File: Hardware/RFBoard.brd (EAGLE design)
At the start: 100 x 100 mm, 327 parts, among them IC1 HMC1097, IC10 NCP702-1.8, IC11 QPC6082, IC12 MCP4812, IC13 QPC6082, IC14 LT5560, IC15 ADF4360, IC16 HMC284, IC17 HMC284, IC18 NCP702-3.3, IC19 NCP702-3.3, IC2 MAX2871, IC20 LT1395, IC21 MAADSS0008, IC22 MAADSS0008, IC23 MAADSS0008, IC24 RFSA2033, IC25 MMG3H21NT1, IC26 MMG3H21NT1, IC27 HMC1021, IC28 MCP4812, IC29 NCP702-3.3, IC3 AP2114HA-3.3, IC30 NCP702-3.3, IC4 NCP702-3.3, IC5 NCP702-3.3, IC6 MAX5873, IC7 NCP702-1.8, IC8 NCP702-3.3, IC9 NCP702-3.3, Q1 BSS123, Q2 BSS123, Q3 BSS123, Q4 BSS123, Q5 BSS123, X1 out

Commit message: Almost all RF routing
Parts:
- removed C157, C158: 1u, rcl:C0603
- removed C22, C23, C24: 33p, rcl:C0603
- removed IC11, IC13: QPC6082, rf:QFN40P200X200X60-15T98
- removed IC30: NCP702-3.3, rf:SOT95P240X110-5
- removed R15, R5, R6: 33, resistor:R0603
- added IC31, IC32: QPC6064, rf:QFN50P400X400X75-25T270
- added L68, L69: (no value), rcl:L2012C
- moved R58 36.4 mm to (15.4, 52.1), flipped to the bottom
- moved R57 29.4 mm to (14.2, 49.0), flipped to the bottom
- moved R56 26.3 mm to (12.0, 49.0), flipped to the bottom, turned to 270 degrees
- moved R55 23.8 mm to (12.8, 51.5), flipped to the bottom, turned to 180 degrees
- moved C60 15.0 mm to (41.0, 86.0), turned to 180 degrees
- moved R16 14.4 mm to (51.8, 50.2)
- moved C29 14.0 mm to (94.0, 51.0), turned to 180 degrees
- moved C59 10.8 mm to (91.5, 69.5), turned to 0 degrees
- moved R54 10.1 mm to (18.0, 40.0), flipped to the bottom
- moved R3 9.63 mm to (51.8, 48.5)
- moved C10 9.51 mm to (65.0, 49.5)
- moved Q1 8.80 mm to (5.50, 73.7)
- moved Q2 6.70 mm to (5.50, 80.0)
- moved C19 6.20 mm to (49.0, 55.0)
- moved R31 5.90 mm to (5.00, 83.6)
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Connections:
- removed net N$19: C22.2, IC2.1, R5.2
- removed net N$21: C24.2, IC2.3, R15.2
- removed net N$24: C23.2, IC2.2, R6.2
- removed net N$89: IC11.8, IC13.10
- removed net STEPPED37: IC11.11, IC13.7
- new net ETOUT: IC27.6
- new net VDD2: C59.1, IC31.16, L68.2
- net +5V: now also L68.1, L69.1; no longer C158.1, IC30.1, IC30.3
- net FILTERED: now also IC32.22; no longer IC13.9
- net GND: now also IC16.9, IC17.9, IC31.1, IC31.10, IC31.12, IC31.13, IC31.15, IC31.20, IC31.21, IC31.23, IC31.25, IC31.3, IC31.4, IC31.6, IC31.7, IC31.9, IC32.1, IC32.10, IC32.12, IC32.13, IC32.15, IC32.20, IC32.21, IC32.23, IC32.25, IC32.3, IC32.4, IC32.6, IC32.7, IC32.9; no longer C157.2, C158.2, C22.1, C23.1, C24.1, IC11.14, IC11.15, IC13.14, IC13.15, IC30.2
- net MOD_OUT: now also IC31.22; no longer IC11.9
- net N$52: now also IC31.2; no longer IC11.12
- net N$53: now also IC32.11; no longer IC13.6
- net N$60: now also IC31.5; no longer IC11.13
- net N$69: now also IC32.5; no longer IC13.13
- net N$76: now also IC31.11; no longer IC11.6
- net N$77: now also IC32.2; no longer IC13.12
- net N$84: now also IC31.14; no longer IC11.7
- net N$85: now also IC32.24; no longer IC13.11
- net N$90: now also IC31.8; no longer IC11.5
- net N$91: now also IC32.8; no longer IC13.5
- net SPI_CLK: now also IC2.1; no longer R5.1
- net SPI_MOSI: now also IC2.2; no longer R6.1
- net STEPPED25: now also IC31.24, IC32.14; no longer IC11.10, IC13.8
- net SW1_CTL1: now also IC31.17; no longer IC11.3
- net SW1_CTL2: now also IC31.18; no longer IC11.2
- net SW1_CTL3: now also IC31.19; no longer IC11.1
- net SW2_CTL1: now also IC32.17; no longer IC13.3
- net SW2_CTL2: now also IC32.18; no longer IC13.2
- net SW2_CTL3: now also IC32.19; no longer IC13.1
- net SWITCHES_VCC: now also IC32.16, L69.2; no longer C157.1, C59.1, IC11.4, IC13.4, IC30.5
- net SYNTH_LE: now also IC2.3; no longer R15.1
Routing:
- net GND: track 0.00 -> 1922.2 mm, vias 0 -> 102
- net +5V: track 0.00 -> 70.8 mm, vias 0 -> 21
- net EN_DIREKT: track 0.00 -> 60.9 mm, vias 0 -> 2
- net SPI_MOSI: track 0.00 -> 51.4 mm, vias 0 -> 7
- net 15DB1: track 0.00 -> 49.6 mm, vias 0 -> 2
- net SPI_CLK: track 0.00 -> 47.4 mm, vias 0 -> 7
- net GAIN_CTRL: track 0.00 -> 45.9 mm, vias 0 -> 2
- net 15DB2: track 0.00 -> 41.3 mm, vias 0 -> 2
- net N$154: track 0.00 -> 39.1 mm, vias 0 -> 4
- net STEPPED37: track 34.1 -> 0.00 mm
- net 15DB3: track 0.00 -> 32.8 mm, vias 0 -> 2
- net N$152: track 0.00 -> 31.9 mm
- net SW_HET: track 0.00 -> 29.1 mm, vias 0 -> 2
- net SW_DIRECT: track 0.00 -> 28.9 mm, vias 0 -> 2
- net PLL_DIG3: track 0.00 -> 27.2 mm, vias 0 -> 4
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- added copper zone on layer 15, net +5V
- added copper zone on layer 1, net GND
- added copper zone on layer 16, net GND
- added copper zone on layer 2, net GND

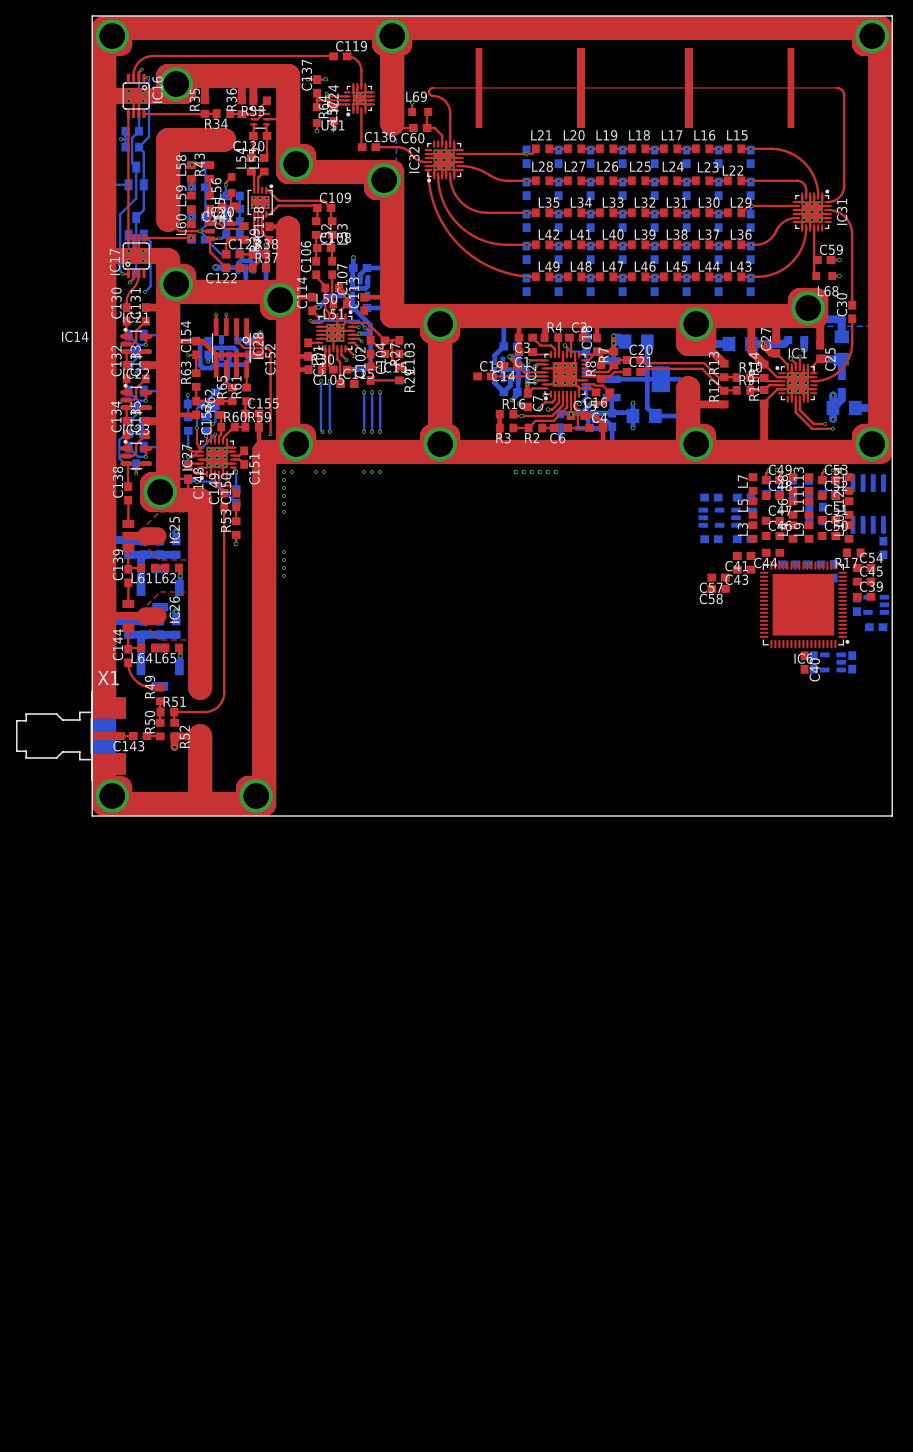
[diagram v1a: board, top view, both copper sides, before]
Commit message: FPGA + power supply added
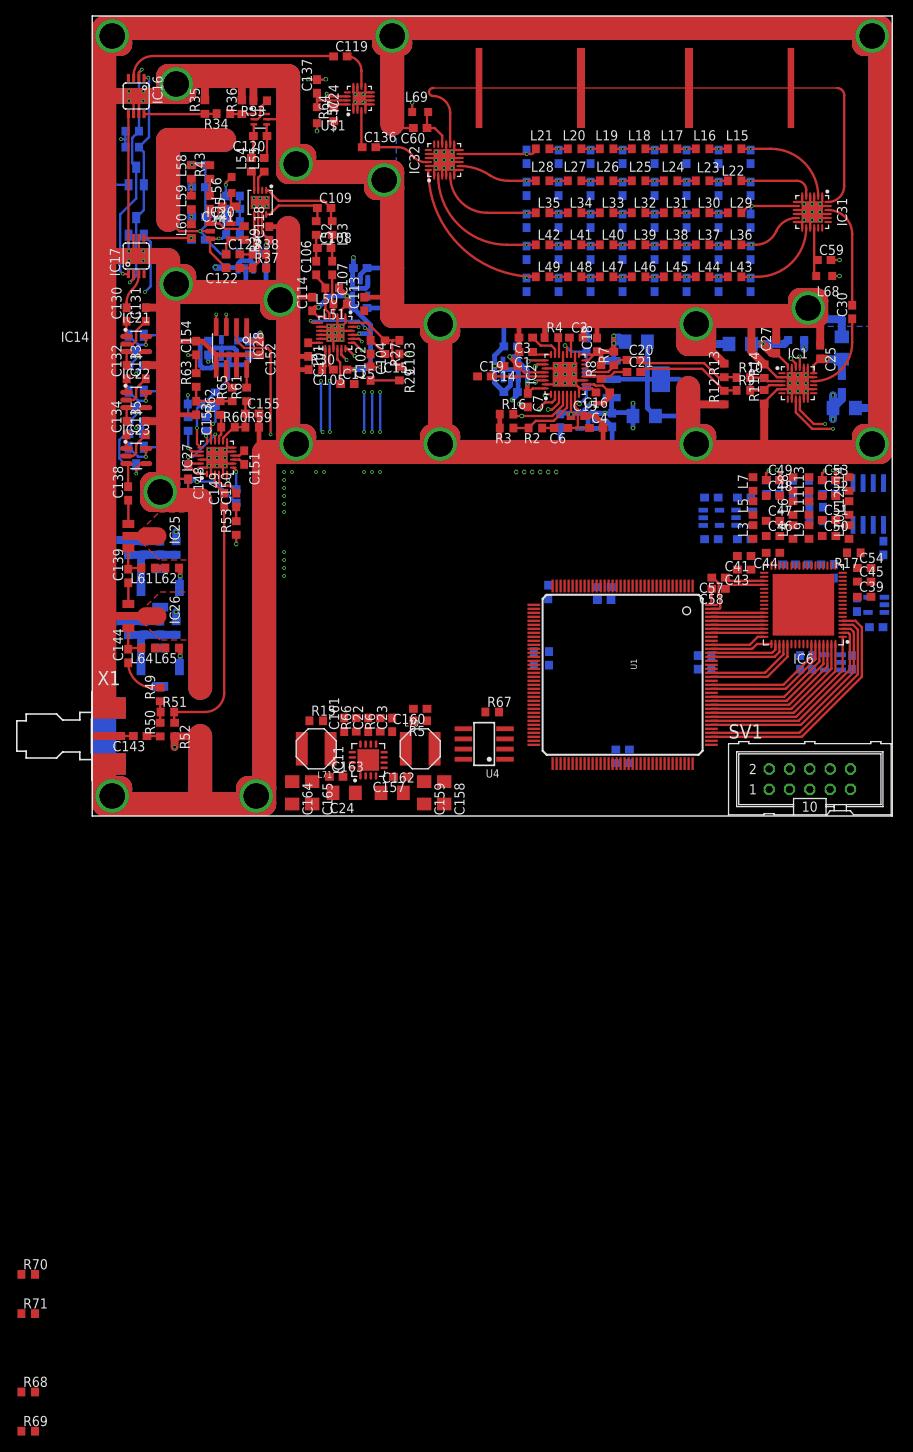
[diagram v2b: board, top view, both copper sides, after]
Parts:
- added C157, C163, C166, C167, C168, C169, C170, C171, C172, C173, C174: 100n, rcl:C0603
- added C158, C159, C164, C165: 22u, rcl:C1206
- added C160: 22p, rcl:C0603
- added C161, C23: 10n, rcl:C0603
- added C162, C24: 10u, rcl:C1206
- added C22: 1u, rcl:C0603
- added IC11: TPS42951, custom-ic:QFN65P400X400X100-17T270
- added L70, L71: 2u2, custom-ic:SRN5040
- added R15, R5: 73k2, resistor:R0603
- added R6, R66: 22k1, resistor:R0603
- added R67: 22, resistor:R0603
- added R68, R69, R70, R71: 10k, resistor:R0603
- added SV1: (no value), con-ml:ML10
- added U1: 6SLX9TQG144, xilinx_devices_V6:TQ144
- added U4: W25Q16BVSN, memory-winbond:SO08
- moved C40 0.55 mm to (88.5, 19.2), flipped to the bottom
- moved C31 0.20 mm to (90.0, 19.2)
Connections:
- new net +3V3: C158.1, C159.1, C160.1, C166.1, C167.1, C168.1, C169.1, C170.1, L70.P$2, R5.1, R68.2, R70.2, R71.2, SV1.4, U1.P122, U1.P125, U1.P129, U1.P135, U1.P20, U1.P36, U1.P42, U1.P53, U1.P63, U1.P69, U1.P90, U4.3, U4.7, U4.8
- new net FLACH_MOSI: U1.P64, U4.5
- new net FLASH_CLK: U1.P70, U4.6
- new net FLASH_CS: U1.P38, U4.1
- new net FLASH_MISO: R67.1, U4.2
- new net N$165: C22.1, IC11.11
- new net N$166: C23.1, IC11.8
- new net N$167: C160.2, IC11.9, R5.2, R6.1
- new net N$168: C161.1, IC11.13
- new net N$169: C157.1, IC11.5, L70.P$1
- new net N$170: C157.2, IC11.4
- new net N$171: IC11.12, R15.2, R66.1
- new net N$172: C163.1, IC11.16, L71.P$1
- new net N$173: C163.2, IC11.1
- new net N$174: R67.2, U1.P65
- new net N$175: R70.1, U1.P71
- new net N$176: R68.1, U1.P37
- new net N$177: R71.1, U1.P39
- new net N$19: SV1.3, U1.P106
- new net N$21: SV1.5, U1.P107
- new net N$24: SV1.9, U1.P110
- new net N$89: SV1.1, U1.P109
- new net VCCINT: C164.1, C165.1, C171.1, C172.1, C173.1, C174.1, L71.P$2, R15.1, U1.P128, U1.P19, U1.P28, U1.P52, U1.P89
- net +5V: now also C162.1, C24.1, IC11.14, IC11.2, IC11.3, IC11.7
- net CLKN: now also U1.P143
- net CLKP: now also R69.2, U1.P144
- net GND: now also C158.2, C159.2, C161.2, C162.2, C164.2, C165.2, C166.2, C167.2, C168.2, C169.2, C170.2, C171.2, C172.2, C173.2, C174.2, C22.2, C23.2, C24.2, IC11.10, IC11.15, IC11.17, IC11.6, R6.2, R66.2, R69.1, SV1.10, SV1.2, U1.P108, U1.P113, U1.P13, U1.P130, U1.P136, U1.P25, U1.P3, U1.P49, U1.P54, U1.P60, U1.P68, U1.P73, U1.P77, U1.P91, U1.P96, U4.4
- net I0: now also U1.P126
- net I1: now also U1.P127
- net I10: now also U1.P141
- net I11: now also U1.P142
- net I2: now also U1.P131
- net I3: now also U1.P132
- net I4: now also U1.P133
- net I5: now also U1.P134
- net I6: now also U1.P137
- net I7: now also U1.P138
- net I8: now also U1.P139
- net I9: now also U1.P140
- net Q0: now also U1.P111
- net Q1: now also U1.P112
- net Q10: now also U1.P123
- net Q11: now also U1.P124
- net Q2: now also U1.P114
- net Q3: now also U1.P115
- net Q4: now also U1.P116
- net Q5: now also U1.P117
- net Q6: now also U1.P118
- net Q7: now also U1.P119
- net Q8: now also U1.P120
- net Q9: now also U1.P121
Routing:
- net Q0: track 0.00 -> 30.8 mm
- net Q1: track 0.00 -> 29.1 mm
- net Q2: track 0.00 -> 27.1 mm
- net Q3: track 0.00 -> 25.3 mm
- net Q4: track 0.00 -> 23.0 mm
- net Q5: track 0.00 -> 21.0 mm
- net Q6: track 0.00 -> 20.2 mm
- net Q7: track 0.00 -> 19.3 mm
- net Q8: track 0.00 -> 18.4 mm
- net Q9: track 0.00 -> 17.5 mm
- net Q10: track 0.00 -> 16.4 mm
- net Q11: track 0.00 -> 15.5 mm
- net I0: track 0.00 -> 12.1 mm
- net I1: track 0.00 -> 11.2 mm
- net I2: track 0.00 -> 9.74 mm
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
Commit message: MCU added
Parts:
- added C175, C176, C177, C178, C179, C180: 100n, rcl:C0603
- added IC13: STM32F030C8T, micro-stm_v3:LQFP48
- added JP1: (no value), pinhead:1X05
- added JP2: (no value), pinhead:1X03
- added Q6: BSS84, transistor-small-signal:SOT23
- added R72, R73: 10k, resistor:R0603
- added SV2: (no value), con-ml:ML10
- added TC1: TCXO-NO-VC-CFPT-127, IQD-Frequency-Products:5.0X3.2-TCXO
- moved R69 138.6 mm to (78.3, 31.6), turned to 180 degrees
- moved R68 116.2 mm to (51.8, 27.6), turned to 180 degrees
- moved R71 110.2 mm to (53.0, 29.6)
- moved R70 88.3 mm to (55.0, 4.50)
- moved C158 21.4 mm to (24.5, 11.7), turned to 90 degrees
- moved C164 20.5 mm to (43.5, 11.7), turned to 90 degrees
- moved C160 18.2 mm to (27.5, 1.20), turned to 0 degrees
- moved C159 17.0 mm to (27.0, 11.7), turned to 90 degrees
- moved R5 16.3 mm to (27.5, 2.70), turned to 0 degrees
- moved C165 16.1 mm to (41.0, 11.7), turned to 90 degrees
- moved R15 15.5 mm to (40.5, 2.70), turned to 180 degrees
- moved L70 13.7 mm to (27.5, 6.20), turned to 180 degrees
- moved L71 12.7 mm to (40.5, 6.20), turned to 0 degrees
- moved C162 10.9 mm to (31.0, 11.7), turned to 180 degrees
- moved C23 10.5 mm to (31.0, 3.20), turned to 270 degrees
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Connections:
- removed net DET_\EN: IC27.7, R54.2
- removed net EN_DIREKT: Q1.1
- new net DET_/EN: IC13.2, IC27.7, R54.2
- new net EN_DIRECT: IC13.12, Q1.1
- new net EN_INTREF: Q6.1, R73.1
- new net N$178: IC13.31, JP2.1
- new net N$179: IC13.30, JP2.3
- new net N$180: IC13.37, JP1.2
- new net N$181: C179.1, Q6.3, TC1.4
- new net N$182: IC13.34, JP1.4
- new net N$183: C178.1, IC13.7, JP1.5, R72.1
- new net N$184: IC13.29, U1.P24
- new net N$185: IC13.25, SV2.2
- new net N$186: IC13.28, SV2.8
- new net N$187: IC13.27, SV2.6
- new net N$188: IC13.26, SV2.4
- net +3V3: now also C175.1, C176.1, C177.1, C180.1, IC13.1, IC13.24, IC13.36, IC13.48, IC13.9, JP1.1, R72.2, U1.P18, U1.P31, U1.P4
- net +5V: now also SV2.1, SV2.3
- net 10MHZ_REF: now also TC1.3
- net 15DB1: now also IC13.6
- net 15DB2: now also IC13.5
- net 15DB3: now also IC13.4
- net ADF_CE: now also IC13.32
- net ADF_LE: now also IC13.38
- net ADF_MUX: now also IC13.33
- net DBM_CS: now also IC13.42
- net DET_SCI1: now also IC13.45
- net DET_SCI2: now also IC13.46
- net DET_SCI3: now also IC13.43
- net DET_SCI4: now also IC13.3
- net GND: now also C175.2, C176.2, C177.2, C178.2, C179.2, C180.2, IC13.23, IC13.35, IC13.44, IC13.47, IC13.8, JP1.3, JP2.2, SV2.5, SV2.7, SV2.9, TC1.2
- net PLL_DIG3: now also Q6.2, R73.2
- net SPI_CLK: now also IC13.41
- net SPI_MOSI: now also IC13.39
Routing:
- net GND: track 1922.2 -> 2165.3 mm, vias 102 -> 176
- net EN_DIRECT: track 0.00 -> 67.2 mm, vias 0 -> 2
- net EN_DIREKT: track 60.9 -> 0.00 mm, vias 2 -> 0
- net +3V3: track 0.00 -> 60.9 mm, vias 0 -> 13
- net VCCINT: track 0.00 -> 42.9 mm, vias 0 -> 9
- net +5V: track 70.8 -> 113.6 mm, vias 21 -> 33
- net N$25: track 0.00 -> 36.9 mm, vias 0 -> 5
- net N$184: track 0.00 -> 31.3 mm, vias 0 -> 2
- net DET_SCI3: track 5.87 -> 33.1 mm, vias 1 -> 2
- net N$154: track 39.1 -> 13.5 mm, vias 4 -> 2
- net N$89: track 0.00 -> 25.5 mm
- net DET_SCI1: track 4.64 -> 28.2 mm, vias 1 -> 2
- net N$24: track 0.00 -> 20.9 mm
- net N$26: track 0.00 -> 20.5 mm, vias 0 -> 2
- net N$21: track 0.00 -> 19.7 mm
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- added copper zone on layer 15, net VCCINT

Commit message: Routing of schematic completed
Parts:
- added C181: 100n, rcl:C0603
- added C182: 33p, rcl:C0603
- added R74: 10k, resistor:R0603
- added R75, R76: 22, resistor:R0603
- moved C178 29.7 mm to (29.0, 29.0), flipped to the bottom, turned to 270 degrees
- moved R72 28.1 mm to (29.0, 33.0), flipped to the bottom, turned to 90 degrees
- moved R71 4.71 mm to (52.0, 25.0), turned to 180 degrees
- moved R70 1.50 mm to (55.0, 6.00)
- moved R68 0.63 mm to (52.0, 27.0)
- moved C177 0.40 mm to (30.5, 31.9)
- moved JP2 0.20 mm to (45.2, 31.3)
- moved Q1 0.20 mm to (5.50, 73.5)
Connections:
- new net FPGA_CS: IC13.16, U1.P35
- new net N$189: C181.1, IC13.10, R74.2
- new net N$190: C182.1, R75.2, U1.P17
- new net N$191: IC13.40, U1.P16
- new net N$192: R76.2, U1.P23
- net 10MHZ_REF: now also R76.1
- net ADF_CE: now also IC13.15; no longer IC13.32
- net ADF_MUX: now also IC13.14; no longer IC13.33
- net EN_INTREF: now also IC13.13
- net ETOUT: now also R74.1
- net GND: now also C181.2, C182.2
- net OFFSET_CS: now also IC13.19
- net SPI_CLK: now also R75.1
- net SPI_MOSI: now also U1.P15
- net SW1_CTL1: now also U1.P1
- net SW1_CTL2: now also U1.P2
- net SW1_CTL3: now also U1.P5
- net SW2_CTL1: now also U1.P6
- net SW2_CTL2: now also U1.P7
- net SW2_CTL3: now also U1.P8
- net SYNTH_CE: now also IC13.32
- net SYNTH_LE: now also IC13.22
- net SYNTH_LOCK_DETECT: now also IC13.33
- net SYNTH_MUX: now also IC13.21
- net SYNTH_RF_EN: now also IC13.20
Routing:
- net OFFSET_CS: track 0.00 -> 97.6 mm, vias 0 -> 3
- net SPI_CLK: track 56.6 -> 142.8 mm, vias 7 -> 8
- net SPI_MOSI: track 60.6 -> 142.7 mm, vias 7 -> 8
- net SW2_CTL1: track 0.00 -> 79.3 mm, vias 0 -> 3
- net SW2_CTL2: track 0.00 -> 78.6 mm, vias 0 -> 3
- net SW2_CTL3: track 0.00 -> 77.8 mm, vias 0 -> 3
- net GND: track 2165.3 -> 2236.7 mm, vias 176 -> 995
- net SW1_CTL3: track 0.00 -> 64.3 mm, vias 0 -> 3
- net SW1_CTL2: track 0.00 -> 62.5 mm, vias 0 -> 3
- net SW1_CTL1: track 0.00 -> 61.0 mm, vias 0 -> 3
- net N$191: track 0.00 -> 42.7 mm, vias 0 -> 4
- net +3V3: track 60.9 -> 102.8 mm, vias 13 -> 24
- net N$183: track 0.00 -> 36.7 mm, vias 0 -> 1
- net SYNTH_LOCK_DETECT: track 2.17 -> 38.0 mm, vias 1 -> 2
- net SYNTH_RF_EN: track 17.7 -> 50.0 mm, vias 2 -> 3
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- added copper zone on layer 15, net +3V3
